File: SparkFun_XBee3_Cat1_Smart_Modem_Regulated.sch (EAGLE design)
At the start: 46 parts, among them J4 QWIIC_RIGHT_ANGLE, U2 AP63203

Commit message: Adds four layer numbers, fixes accidental naming of GND to "OPEN"
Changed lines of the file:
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@@
-</segment>
-</net>
-<net name="GND" class="0">
-<segment>
-<pinref part="J4" gate="G$1" pin="1"/>
-<wire x1="228.6" y1="393.7" x2="231.14" y2="393.7" width="0.1524" layer="91"/>
-<wire x1="231.14" y1="393.7" x2="231.14" y2="391.16" width="0.1524" layer="91"/>
-<pinref part="GND16" gate="1" pin="GND"/>
-</segment>
-<segment>
-<pinref part="S1" gate="G$1" pin="3"/>
-<wire x1="45.72" y1="332.74" x2="48.26" y2="332.74" width="0.1524" layer="91"/>
-<wire x1="48.26" y1="332.74" x2="50.8" y2="332.74" width="0.1524" layer="91"/>
-<wire x1="50.8" y1="332.74" x2="50.8" y2="330.2" width="0.1524" layer="91"/>
-<pinref part="GND1" gate="1" pin="GND"/>
-<pinref part="S1" gate="G$1" pin="4"/>
-<wire x1="45.72" y1="330.2" x2="48.26" y2="330.2" width="0.1524" layer="91"/>
-<wire x1="48.26" y1="330.2" x2="48.26" y2="332.74" width="0.1524" layer="91"/>
-<junction x="48.26" y="332.74"/>
-</segment>
-<segment>
-<pinref part="S2" gate="G$1" pin="3"/>
-<wire x1="45.72" y1="347.98" x2="48.26" y2="347.98" width="0.1524" layer="91"/>
-<wire x1="48.26" y1="347.98" x2="50.8" y2="347.98" width="0.1524" layer="91"/>
-<wire x1="50.8" y1="347.98" x2="50.8" y2="345.44" width="0.1524" layer="91"/>
-<pinref part="S2" gate="G$1" pin="4"/>
-<wire x1="48.26" y1="347.98" x2="48.26" y2="345.44" width="0.1524" layer="91"/>
-<wire x1="48.26" y1="345.44" x2="45.72" y2="345.44" width="0.1524" layer="91"/>
-<junction x="48.26" y="347.98"/>
-<pinref part="GND2" gate="1" pin="GND"/>
-</segment>
-<segment>
-<wire x1="58.42" y1="449.58" x2="60.96" y2="449.58" width="0.1524" layer="91"/>
-<wire x1="58.42" y1="447.04" x2="58.42" y2="449.58" width="0.1524" layer="91"/>
-<pinref part="GND22" gate="1" pin="GND"/>
-<pinref part="J2" gate="G$1" pin="GND"/>
-</segment>
-<segment>
-<pinref part="ALED" gate="G$1" pin="1"/>
-<pinref part="GND14" gate="1" pin="GND"/>
-<wire x1="43.18" y1="368.3" x2="43.18" y2="365.76" width="0.1524" layer="91"/>
-</segment>
-<segment>
-<pinref part="PLED" gate="G$1" pin="1"/>
-<pinref part="GND12" gate="1" pin="GND"/>
-<wire x1="27.94" y1="368.3" x2="27.94" y2="365.76" width="0.1524" layer="91"/>
-</segment>
-<segment>
-<pinref part="C1" gate="G$1" pin="2"/>
-<wire x1="157.48" y1="459.74" x2="157.48" y2="462.28" width="0.1524" layer="91"/>
-<pinref part="GND3" gate="1" pin="GND"/>
-</segment>
-<segment>
-<pinref part="U2" gate="G$1" pin="GND"/>
-<wire x1="175.26" y1="464.82" x2="172.72" y2="464.82" width="0.1524" layer="91"/>
-<wire x1="172.72" y1="464.82" x2="172.72" y2="459.74" width="0.1524" layer="91"/>
-<pinref part="GND21" gate="1" pin="GND"/>
-</segment>
-<segment>
-<pinref part="C4" gate="G$1" pin="2"/>
-<wire x1="233.68" y1="459.74" x2="233.68" y2="457.2" width="0.1524" layer="91"/>
-<pinref part="GND15" gate="1" pin="GND"/>
-</segment>
-<segment>
-<pinref part="C2" gate="G$1" pin="2"/>
-<pinref part="GND13" gate="1" pin="GND"/>
-<wire x1="226.06" y1="459.74" x2="226.06" y2="457.2" width="0.1524" layer="91"/>
-</segment>
-<segment>
-<pinref part="C7" gate="G$1" pin="2"/>
-<pinref part="GND10" gate="1" pin="GND"/>
-<wire x1="22.86" y1="462.28" x2="22.86" y2="459.74" width="0.1524" layer="91"/>
-</segment>
-<segment>
-<pinref part="C9" gate="G$1" pin="2"/>
-<pinref part="GND9" gate="1" pin="GND"/>
-<wire x1="27.94" y1="462.28" x2="27.94" y2="459.74" width="0.1524" layer="91"/>
-</segment>
-<segment>
-<pinref part="C6" gate="G$1" pin="2"/>
-<pinref part="GND11" gate="1" pin="GND"/>
-<wire x1="129.54" y1="464.82" x2="129.54" y2="467.36" width="0.1524" layer="91"/>
-</segment>
-<segment>
-<pinref part="GND35" gate="1" pin="GND"/>
-<pinref part="C10" gate="G$1" pin="2"/>
-<wire x1="33.02" y1="459.74" x2="33.02" y2="462.28" width="0.1524" layer="91"/>
-</segment>
-<segment>
-<pinref part="RLED" gate="G$1" pin="1"/>
-<pinref part="GND7" gate="1" pin="GND"/>
-<wire x1="48.26" y1="368.3" x2="48.26" y2="365.76" width="0.1524" layer="91"/>
-</segment>
-<segment>
-<wire x1="104.14" y1="373.38" x2="104.14" y2="368.3" width="0.1524" layer="91"/>
-<pinref part="GND17" gate="1" pin="GND"/>
-<pinref part="J6" gate="J1" pin="10"/>
-<wire x1="104.14" y1="373.38" x2="96.52" y2="373.38" width="0.1524" layer="91"/>
-</segment>
-<segment>
-<pinref part="C5" gate="G$1" pin="2"/>
-<wire x1="17.78" y1="462.28" x2="17.78" y2="459.74" width="0.1524" layer="91"/>
-<pinref part="GND4" gate="1" pin="GND"/>
-</segment>
-<segment>
-<pinref part="C8" gate="G$1" pin="2"/>
-<wire x1="12.7" y1="462.28" x2="12.7" y2="459.74" width="0.1524" layer="91"/>
-<pinref part="GND5" gate="1" pin="GND"/>
 </segment>
 </net>
@@
 </segment>
 </net>
+<net name="GND" class="0">
+<segment>
+<pinref part="C1" gate="G$1" pin="2"/>
+<pinref part="GND3" gate="1" pin="GND"/>
+<wire x1="157.48" y1="462.28" x2="157.48" y2="459.74" width="0.1524" layer="91"/>
+</segment>
+<segment>
+<pinref part="J4" gate="G$1" pin="1"/>
+<wire x1="228.6" y1="393.7" x2="231.14" y2="393.7" width="0.1524" layer="91"/>
+<wire x1="231.14" y1="393.7" x2="231.14" y2="391.16" width="0.1524" layer="91"/>
+<pinref part="GND16" gate="1" pin="GND"/>
+</segment>
+<segment>
+<pinref part="S1" gate="G$1" pin="3"/>
+<wire x1="45.72" y1="332.74" x2="48.26" y2="332.74" width="0.1524" layer="91"/>
+<wire x1="48.26" y1="332.74" x2="50.8" y2="332.74" width="0.1524" layer="91"/>
+<wire x1="50.8" y1="332.74" x2="50.8" y2="330.2" width="0.1524" layer="91"/>
+<pinref part="GND1" gate="1" pin="GND"/>
+<pinref part="S1" gate="G$1" pin="4"/>
+<wire x1="45.72" y1="330.2" x2="48.26" y2="330.2" width="0.1524" layer="91"/>
+<wire x1="48.26" y1="330.2" x2="48.26" y2="332.74" width="0.1524" layer="91"/>
+<junction x="48.26" y="332.74"/>
+</segment>
+<segment>
+<pinref part="S2" gate="G$1" pin="3"/>
+<wire x1="45.72" y1="347.98" x2="48.26" y2="347.98" width="0.1524" layer="91"/>
+<wire x1="48.26" y1="347.98" x2="50.8" y2="347.98" width="0.1524" layer="91"/>
+<wire x1="50.8" y1="347.98" x2="50.8" y2="345.44" width="0.1524" layer="91"/>
+<pinref part="S2" gate="G$1" pin="4"/>
+<wire x1="48.26" y1="347.98" x2="48.26" y2="345.44" width="0.1524" layer="91"/>
+<wire x1="48.26" y1="345.44" x2="45.72" y2="345.44" width="0.1524" layer="91"/>
+<junction x="48.26" y="347.98"/>
+<pinref part="GND2" gate="1" pin="GND"/>
+</segment>
+<segment>
+<wire x1="58.42" y1="449.58" x2="60.96" y2="449.58" width="0.1524" layer="91"/>
+<wire x1="58.42" y1="447.04" x2="58.42" y2="449.58" width="0.1524" layer="91"/>
+<pinref part="GND22" gate="1" pin="GND"/>
+<pinref part="J2" gate="G$1" pin="GND"/>
+</segment>
+<segment>
+<pinref part="ALED" gate="G$1" pin="1"/>
+<pinref part="GND14" gate="1" pin="GND"/>
+<wire x1="43.18" y1="368.3" x2="43.18" y2="365.76" width="0.1524" layer="91"/>
+</segment>
+<segment>
+<pinref part="PLED" gate="G$1" pin="1"/>
+<pinref part="GND12" gate="1" pin="GND"/>
+<wire x1="27.94" y1="368.3" x2="27.94" y2="365.76" width="0.1524" layer="91"/>
+</segment>
+<segment>
+<pinref part="U2" gate="G$1" pin="GND"/>
+<wire x1="175.26" y1="464.82" x2="172.72" y2="464.82" width="0.1524" layer="91"/>
+<wire x1="172.72" y1="464.82" x2="172.72" y2="459.74" width="0.1524" layer="91"/>
+<pinref part="GND21" gate="1" pin="GND"/>
+</segment>
+<segment>
+<pinref part="C4" gate="G$1" pin="2"/>
+<wire x1="233.68" y1="459.74" x2="233.68" y2="457.2" width="0.1524" layer="91"/>
+<pinref part="GND15" gate="1" pin="GND"/>
+</segment>
+<segment>
+<pinref part="C2" gate="G$1" pin="2"/>
+<pinref part="GND13" gate="1" pin="GND"/>
+<wire x1="226.06" y1="459.74" x2="226.06" y2="457.2" width="0.1524" layer="91"/>
+</segment>
+<segment>
+<pinref part="C7" gate="G$1" pin="2"/>
+<pinref part="GND10" gate="1" pin="GND"/>
+<wire x1="22.86" y1="462.28" x2="22.86" y2="459.74" width="0.1524" layer="91"/>
+</segment>
+<segment>
+<pinref part="C9" gate="G$1" pin="2"/>
+<pinref part="GND9" gate="1" pin="GND"/>
+<wire x1="27.94" y1="462.28" x2="27.94" y2="459.74" width="0.1524" layer="91"/>
+</segment>
+<segment>
+<pinref part="C6" gate="G$1" pin="2"/>
+<pinref part="GND11" gate="1" pin="GND"/>
+<wire x1="129.54" y1="464.82" x2="129.54" y2="467.36" width="0.1524" layer="91"/>
+</segment>
+<segment>
+<pinref part="GND35" gate="1" pin="GND"/>
+<pinref part="C10" gate="G$1" pin="2"/>
+<wire x1="33.02" y1="459.74" x2="33.02" y2="462.28" width="0.1524" layer="91"/>
+</segment>
+<segment>
+<pinref part="RLED" gate="G$1" pin="1"/>
+<pinref part="GND7" gate="1" pin="GND"/>
+<wire x1="48.26" y1="368.3" x2="48.26" y2="365.76" width="0.1524" layer="91"/>
+</segment>
+<segment>
+<wire x1="104.14" y1="373.38" x2="104.14" y2="368.3" width="0.1524" layer="91"/>
+<pinref part="GND17" gate="1" pin="GND"/>
+<pinref part="J6" gate="J1" pin="10"/>
+<wire x1="104.14" y1="373.38" x2="96.52" y2="373.38" width="0.1524" layer="91"/>
+</segment>
+<segment>
+<pinref part="C5" gate="G$1" pin="2"/>
+<wire x1="17.78" y1="462.28" x2="17.78" y2="459.74" width="0.1524" layer="91"/>
+<pinref part="GND4" gate="1" pin="GND"/>
+</segment>
+<segment>
+<pinref part="C8" gate="G$1" pin="2"/>
+<wire x1="12.7" y1="462.28" x2="12.7" y2="459.74" width="0.1524" layer="91"/>
+<pinref part="GND5" gate="1" pin="GND"/>
+</segment>
+</net>

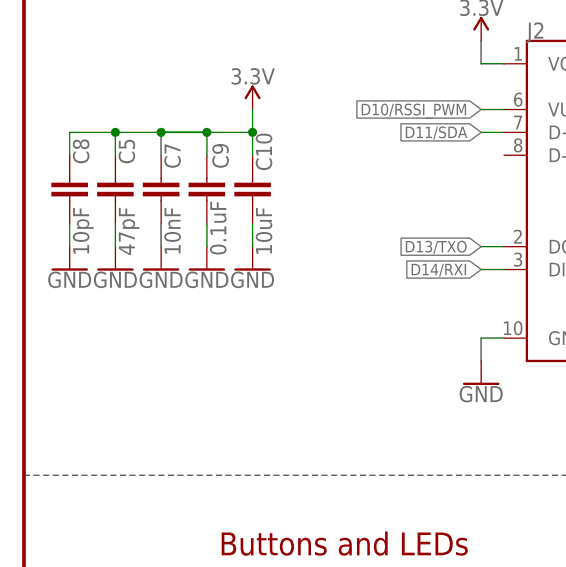
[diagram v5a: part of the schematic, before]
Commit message: Adds vias, fixes acid traps, moves LEDs away from the edge
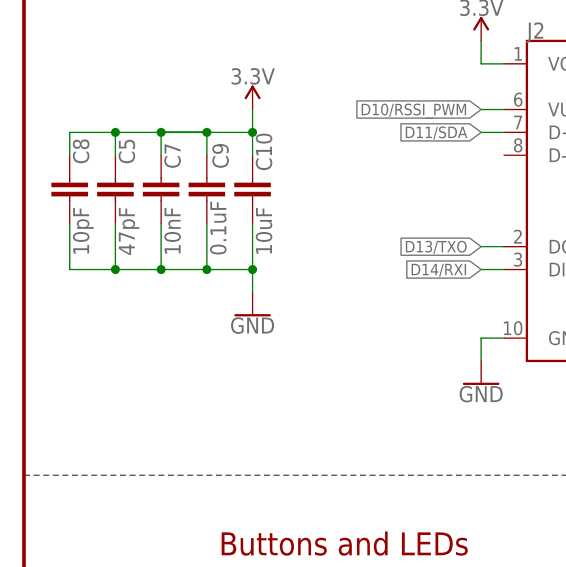
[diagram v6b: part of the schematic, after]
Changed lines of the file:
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@@
 <part name="C7" library="SparkFun-Capacitors" deviceset="10NF" device="-0603-50V-10%" value="10nF"/>
 <part name="C9" library="SparkFun-Capacitors" deviceset="0.1UF" device="-0603-25V-(+80/-20%)" value="0.1uF"/>
-<part name="GND9" library="SparkFun-PowerSymbols" deviceset="GND" device=""/>
-<part name="GND10" library="SparkFun-PowerSymbols" deviceset="GND" device=""/>
 <part name="GND11" library="SparkFun-PowerSymbols" deviceset="GND" device=""/>
 <part name="C10" library="SparkFun-Capacitors" deviceset="10UF" device="-0603-6.3V-20%" value="10uF"/>
@@
 <part name="C5" library="SparkFun-Capacitors" deviceset="47PF" device="-0603-50V-5%" value="47pF"/>
 <part name="C8" library="SparkFun-Capacitors" deviceset="10PF" device="-0603-50V-5%" value="10pF"/>
-<part name="GND4" library="SparkFun-PowerSymbols" deviceset="GND" device=""/>
-<part name="GND5" library="SparkFun-PowerSymbols" deviceset="GND" device=""/>
 <part name="LOGO1" library="SparkFun-Aesthetics" deviceset="SPECIAL_INSTRUCTIONS" device="-ORDERING"/>
 <part name="LOGO4" library="SparkFun-Aesthetics" deviceset="SFE_LOGO_NAME" device="BLANK"/>
@@
 <attribute name="VALUE" x="30.099" y="458.724" size="1.778" layer="96" font="vector" rot="R90"/>
 </instance>
-<instance part="GND9" gate="1" x="27.94" y="457.2" smashed="yes" rot="MR0">
-<attribute name="VALUE" x="27.94" y="456.946" size="1.778" layer="96" font="vector" rot="MR0" align="top-center"/>
-</instance>
-<instance part="GND10" gate="1" x="22.86" y="457.2" smashed="yes" rot="MR0">
-<attribute name="VALUE" x="22.86" y="456.946" size="1.778" layer="96" font="vector" rot="MR0" align="top-center"/>
-</instance>
 <instance part="GND11" gate="1" x="129.54" y="462.28" smashed="yes" rot="MR0">
 <attribute name="VALUE" x="129.54" y="462.026" size="1.778" layer="96" font="vector" rot="MR0" align="top-center"/>
@@
 <attribute name="VALUE" x="33.02" y="477.774" size="1.778" layer="96" font="vector" rot="MR0" align="bottom-center"/>
 </instance>
-<instance part="GND35" gate="1" x="33.02" y="457.2" smashed="yes" rot="MR0">
-<attribute name="VALUE" x="33.02" y="456.946" size="1.778" layer="96" font="vector" rot="MR0" align="top-center"/>
+<instance part="GND35" gate="1" x="33.02" y="452.12" smashed="yes" rot="MR0">
+<attribute name="VALUE" x="33.02" y="451.866" size="1.778" layer="96" font="vector" rot="MR0" align="top-center"/>
 </instance>
 <instance part="H1" gate="G$1" x="246.38" y="350.52" smashed="yes"/>
@@
 <attribute name="NAME" x="14.859" y="468.884" size="1.778" layer="95" font="vector" rot="R90"/>
 <attribute name="VALUE" x="14.859" y="458.724" size="1.778" layer="96" font="vector" rot="R90"/>
-</instance>
-<instance part="GND4" gate="1" x="17.78" y="457.2" smashed="yes" rot="MR0">
-<attribute name="VALUE" x="17.78" y="456.946" size="1.778" layer="96" font="vector" rot="MR0" align="top-center"/>
-</instance>
-<instance part="GND5" gate="1" x="12.7" y="457.2" smashed="yes" rot="MR0">
-<attribute name="VALUE" x="12.7" y="456.946" size="1.778" layer="96" font="vector" rot="MR0" align="top-center"/>
 </instance>
 <instance part="LOGO1" gate="G$1" x="219.71" y="325.374" smashed="yes"/>
@@
 </segment>
 <segment>
-<pinref part="C7" gate="G$1" pin="2"/>
-<pinref part="GND10" gate="1" pin="GND"/>
-<wire x1="22.86" y1="462.28" x2="22.86" y2="459.74" width="0.1524" layer="91"/>
-</segment>
-<segment>
-<pinref part="C9" gate="G$1" pin="2"/>
-<pinref part="GND9" gate="1" pin="GND"/>
-<wire x1="27.94" y1="462.28" x2="27.94" y2="459.74" width="0.1524" layer="91"/>
-</segment>
-<segment>
 <pinref part="C6" gate="G$1" pin="2"/>
 <pinref part="GND11" gate="1" pin="GND"/>
@@
 <pinref part="GND35" gate="1" pin="GND"/>
 <pinref part="C10" gate="G$1" pin="2"/>
-<wire x1="33.02" y1="459.74" x2="33.02" y2="462.28" width="0.1524" layer="91"/>
+<wire x1="33.02" y1="454.66" x2="33.02" y2="457.2" width="0.1524" layer="91"/>
+<pinref part="C8" gate="G$1" pin="2"/>
+<wire x1="33.02" y1="457.2" x2="33.02" y2="462.28" width="0.1524" layer="91"/>
+<wire x1="12.7" y1="462.28" x2="12.7" y2="457.2" width="0.1524" layer="91"/>
+<wire x1="12.7" y1="457.2" x2="17.78" y2="457.2" width="0.1524" layer="91"/>
+<junction x="33.02" y="457.2"/>
+<pinref part="C5" gate="G$1" pin="2"/>
+<wire x1="17.78" y1="457.2" x2="22.86" y2="457.2" width="0.1524" layer="91"/>
+<wire x1="22.86" y1="457.2" x2="27.94" y2="457.2" width="0.1524" layer="91"/>
+<wire x1="27.94" y1="457.2" x2="33.02" y2="457.2" width="0.1524" layer="91"/>
+<wire x1="17.78" y1="462.28" x2="17.78" y2="457.2" width="0.1524" layer="91"/>
+<junction x="17.78" y="457.2"/>
+<pinref part="C7" gate="G$1" pin="2"/>
+<wire x1="22.86" y1="462.28" x2="22.86" y2="457.2" width="0.1524" layer="91"/>
+<junction x="22.86" y="457.2"/>
+<pinref part="C9" gate="G$1" pin="2"/>
+<wire x1="27.94" y1="462.28" x2="27.94" y2="457.2" width="0.1524" layer="91"/>
+<junction x="27.94" y="457.2"/>
 </segment>
 <segment>
@@
 <wire x1="104.14" y1="373.38" x2="96.52" y2="373.38" width="0.1524" layer="91"/>
 </segment>
-<segment>
-<pinref part="C5" gate="G$1" pin="2"/>
-<wire x1="17.78" y1="462.28" x2="17.78" y2="459.74" width="0.1524" layer="91"/>
-<pinref part="GND4" gate="1" pin="GND"/>
-</segment>
-<segment>
-<pinref part="C8" gate="G$1" pin="2"/>
-<wire x1="12.7" y1="462.28" x2="12.7" y2="459.74" width="0.1524" layer="91"/>
-<pinref part="GND5" gate="1" pin="GND"/>
-</segment>
-</net>
+</net>

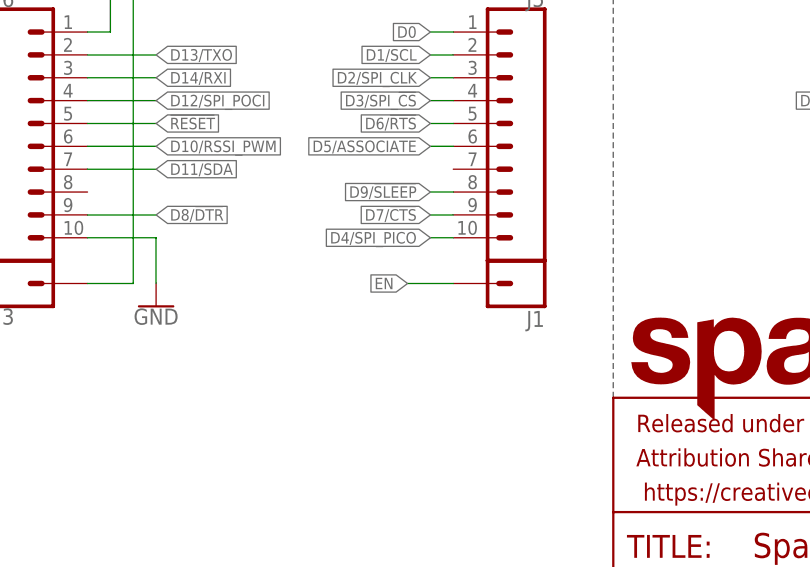
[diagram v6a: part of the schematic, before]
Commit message: Moves I2C jumper down to make more space for the silk in that area
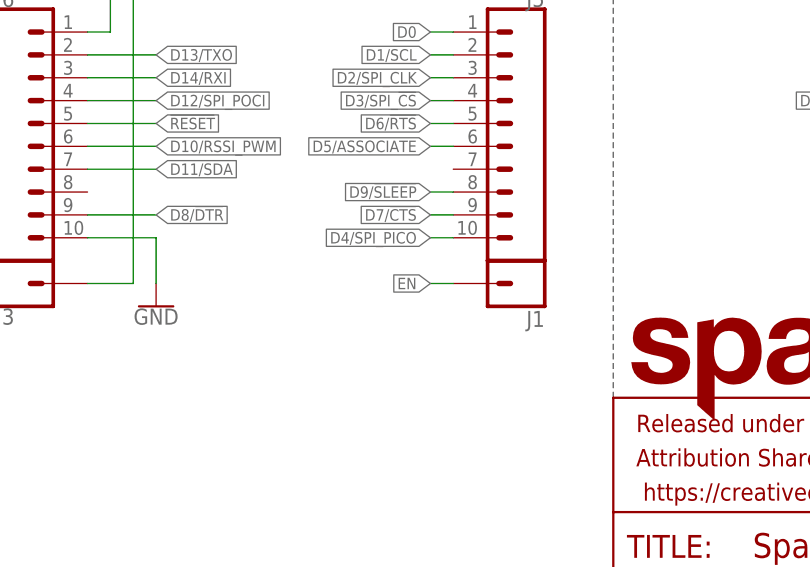
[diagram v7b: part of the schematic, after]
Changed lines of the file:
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@@
 </segment>
 <segment>
-<wire x1="132.08" y1="368.3" x2="137.16" y2="368.3" width="0.1524" layer="91"/>
-<label x="132.08" y="368.3" size="1.27" layer="95" font="vector" rot="R180" xref="yes"/>
+<wire x1="134.62" y1="368.3" x2="137.16" y2="368.3" width="0.1524" layer="91"/>
+<label x="134.62" y="368.3" size="1.27" layer="95" font="vector" rot="R180" xref="yes"/>
 <pinref part="J1" gate="G$1" pin="1"/>
 </segment>
